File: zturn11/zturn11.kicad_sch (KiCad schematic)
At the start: 138 parts, among them J1 2x18edgecon, J11 Conn_02x40_Odd_Even, J12 Conn_02x40_Odd_Even, J2 2x18edgecon, J3 2x18edgecon, J4 2x18edgecon, J5 Conn_01x16, J7 Conn_01x03, Q1 SSM6N15AFU, Q10 SSM6N15AFU, Q11 SSM6N15AFU, Q12 SSM6N15AFU, Q13 SSM6N15AFU, Q14 SSM6N15AFU, Q15 SSM6N15AFU, Q16 SSM6N15AFU, Q17 SSM6N15AFU, Q18 SSM6N15AFU, Q19 SSM6N15AFU, Q2 SSM6N15AFU, Q20 SSM6N15AFU, Q21 SSM6N15AFU, Q22 SSM6N15AFU, Q23 SSM6N15AFU, Q24 SSM6N15AFU, Q25 SSM6N15AFU, Q26 SSM6N15AFU, Q27 SSM6N15AFU, Q28 SSM6N15AFU, Q29 SSM6N15AFU, Q3 SSM6N15AFU, Q30 SSM6N15AFU, Q31 SSM6N15AFU, Q32 SSM6N15AFU, Q33 SSM6N15AFU, Q34 SSM6N15AFU, Q35 SSM6N15AFU, Q36 SSM6N15AFU, Q37 SSM6N15AFU, Q38 SSM6N15AFU, Q39 SSM6N15AFU, Q4 SSM6N15AFU, Q40 SSM6N15AFU, Q41 SSM6N15AFU, Q42 SSM6N15AFU, Q43 SSM6N15AFU, Q44 SSM6N15AFU, Q5 SSM6N15AFU, Q50 SSM6N15AFU, Q51 SSM6N15AFU, Q52 SSM6N15AFU, Q53 SSM6N15AFU, Q54 SSM6N15AFU, Q55 SSM6N15AFU, Q56 SSM6N15AFU, Q57 SSM6N15AFU, Q58 SSM6N15AFU, Q59 SSM6N15AFU, Q6 SSM6N15AFU, Q60 SSM6N15AFU, Q61 SSM6N15AFU, Q62 SSM6N15AFU, Q63 SSM6N15AFU, Q64 SSM6N15AFU, Q7 SSM6N15AFU, Q8 SSM6N15AFU, Q9 SSM6N15AFU

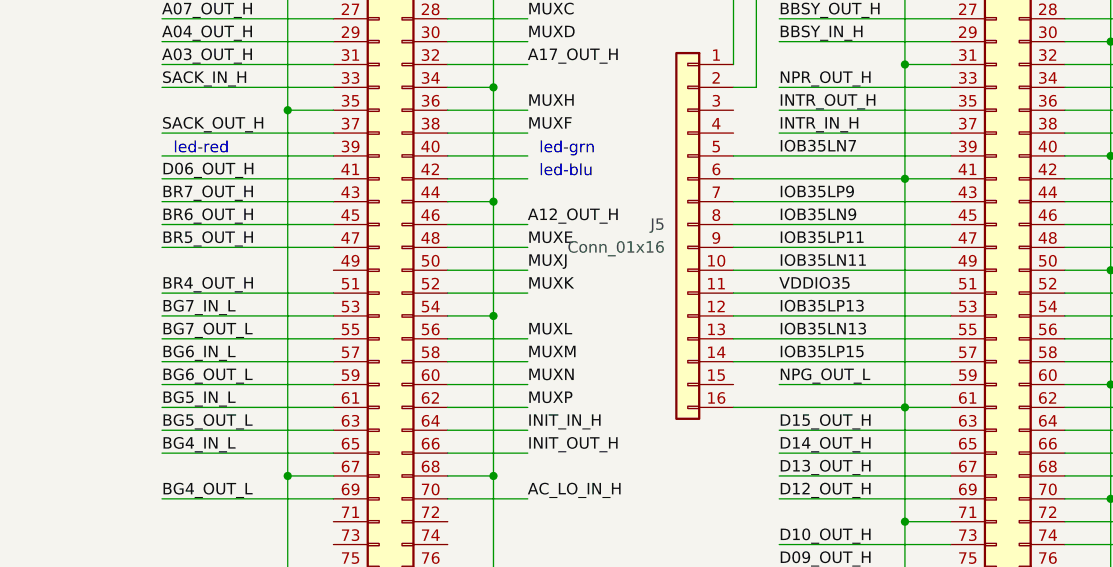
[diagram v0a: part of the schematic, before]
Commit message: update pcb with patch for BG6_OUT_H
also move power connector out from under zturn board
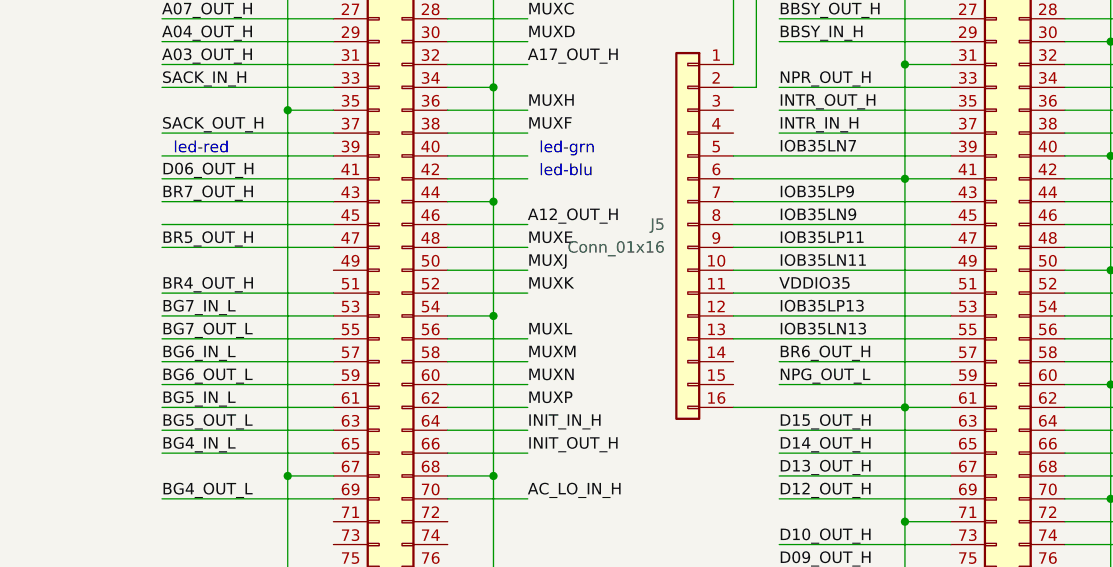
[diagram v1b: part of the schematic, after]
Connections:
- net BR6_OUT_H: now also J12.57 (Pin_57); no longer J11.45 (Pin_45)
- net IOB35LP15: no longer names the net of J5.14 (Pin_14)
- net IOB35LP15: no longer J12.57 (Pin_57)
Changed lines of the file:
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@@
+    (stroke (width 0) (type default))
+  )
+  (wire (pts (xy 334.01 111.76) (xy 353.06 111.76))
     (stroke (width 0) (type default))
   )
@@
     (stroke (width 0) (type default))
   )
-  (wire (pts (xy 328.93 111.76) (xy 353.06 111.76))
-    (stroke (width 0) (type default))
-  )
   (wire (pts (xy 403.86 400.05) (xy 411.48 400.05))
     (stroke (width 0) (type default))
@@
     (effects (font (size 1.27 1.27)) (justify left bottom))
   )
-  (label "IOB35LP15" (at 334.01 111.76 0) (fields_autoplaced)
-    (effects (font (size 1.27 1.27)) (justify left bottom))
-  )
   (label "BUS_A17_L" (at 121.92 27.94 0) (fields_autoplaced)
     (effects (font (size 1.27 1.27)) (justify left bottom))
@@
     (effects (font (size 1.27 1.27)) (justify left bottom))
   )
-  (label "BR6_OUT_H" (at 265.43 96.52 0) (fields_autoplaced)
-    (effects (font (size 1.27 1.27)) (justify left bottom))
-  )
+  (label "BR6_OUT_H" (at 334.01 111.76 0) (fields_autoplaced)
+    (effects (font (size 1.27 1.27)) (justify left bottom))
+  )

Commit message: add diodes to the zturn11 board so the muxes work
also add AC_LO_OUT_H and DC_LO_OUT_H drivers
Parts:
- added C20: 0.1u, Capacitor_SMD:C_0402_1005Metric, symbol Device:C
- added D1, D10, D11, D12, D13, D14, D15, D16, D17, D18, D19, D2, D20, D21, D22, D23, D24, D25, D26, D27, D28, D29, D3, D30, D31, D32, D33, D34, D35, D36, D37, D38, D39, D4, D40, D41, D42, D43, D44, D5, D6, D7, D8, D9: RB521S-30, Diode_SMD:D_SOD-523, symbol Device:D_Schottky_Small
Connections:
- net +3V3: now also J5.4 (Pin_4), C20.1
- net BR6_OUT_H: now also J11.43 (Pin_43); no longer J12.57 (Pin_57)
- net BR7_OUT_H: now also J11.41 (Pin_41); no longer J11.43 (Pin_43)
- net BUS_AC_LO_L: now also Q8.3 (D2)
- net BUS_DC_LO_L: now also Q4.3 (D2)
- net D00_OUT_H: now also J12.58 (Pin_58); no longer J12.56 (Pin_56)
- net D01_OUT_H: now also J12.62 (Pin_62); no longer J12.58 (Pin_58)
- net D02_OUT_H: now also J12.54 (Pin_54); no longer J12.52 (Pin_52)
- net D03_OUT_H: now also J12.56 (Pin_56); no longer J12.54 (Pin_54)
- net D04_OUT_H: now also J12.66 (Pin_66); no longer J12.64 (Pin_64)
- net D05_OUT_H: now also J12.64 (Pin_64); no longer J12.62 (Pin_62)
- net D06_OUT_H: now also J12.52 (Pin_52); no longer J11.41 (Pin_41)
- net D07_OUT_H: now also J12.77 (Pin_77); no longer J12.66 (Pin_66)
- net D08_OUT_H: now also J12.75 (Pin_75); no longer J12.77 (Pin_77)
- net D09_OUT_H: now also J12.73 (Pin_73); no longer J12.75 (Pin_75)
- net D10_OUT_H: now also J12.69 (Pin_69); no longer J12.73 (Pin_73)
- net D11_OUT_H: now also J12.79 (Pin_79); no longer J12.76 (Pin_76)
- net D12_OUT_H: now also J12.67 (Pin_67); no longer J12.69 (Pin_69)
- net D13_OUT_H: now also J12.65 (Pin_65); no longer J12.67 (Pin_67)
- net D14_OUT_H: now also J12.59 (Pin_59); no longer J12.65 (Pin_65)
- net D15_OUT_H: now also J12.55 (Pin_55); no longer J12.63 (Pin_63)
- net DC_LO_IN_H: now also J12.76 (Pin_76); no longer J12.74 (Pin_74)
- net GND: now also C20.2
- net HLTGR_IN_L: now also J12.72 (Pin_72); no longer J12.68 (Pin_68)
- net HLTRQ_OUT_H: now also J12.74 (Pin_74); no longer J12.72 (Pin_72)
- net MUXA: now also D1.2 (A), D5.2 (A), D8.2 (A); no longer Q10.6 (D1), Q14.6 (D1), Q2.6 (D1)
- net MUXB: now also D2.2 (A), D6.2 (A), D9.2 (A); no longer Q11.6 (D1), Q16.6 (D1), Q3.6 (D1)
- net MUXC: now also D10.2 (A), D3.2 (A), D7.2 (A); no longer Q13.6 (D1), Q17.6 (D1), Q5.6 (D1)
- net MUXD: now also D11.2 (A), D27.2 (A), D4.2 (A); no longer Q18.6 (D1), Q36.6 (D1), Q7.6 (D1)
- net MUXE: now also D12.2 (A), D23.2 (A), D28.2 (A); no longer Q19.6 (D1), Q25.6 (D1), Q37.6 (D1)
- net MUXF: now also D13.2 (A), D22.2 (A), D29.2 (A); no longer Q20.6 (D1), Q26.6 (D1), Q38.6 (D1)
- net MUXH: now also D14.2 (A), D21.2 (A), D30.2 (A); no longer Q21.6 (D1), Q27.6 (D1), Q39.6 (D1)
- net MUXJ: now also D15.2 (A), D20.2 (A), D31.2 (A); no longer Q23.6 (D1), Q28.6 (D1), Q40.6 (D1)
- net MUXK: now also D19.2 (A), D35.2 (A), D42.2 (A); no longer Q29.6 (D1), Q41.6 (D1), Q57.6 (D1)
- net MUXL: now also D18.2 (A), D36.2 (A), D43.2 (A); no longer Q30.6 (D1), Q42.6 (D1), Q58.6 (D1)
- net MUXM: now also D17.2 (A), D37.2 (A), D44.2 (A); no longer Q31.6 (D1), Q43.6 (D1), Q59.6 (D1)
- net MUXN: now also D16.2 (A), D34.2 (A), D38.2 (A); no longer Q32.6 (D1), Q54.6 (D1), Q60.6 (D1)
- net MUXP: now also D24.2 (A), D33.2 (A), D39.2 (A); no longer Q33.6 (D1), Q55.6 (D1), Q61.6 (D1)
- net MUXR: now also D25.2 (A), D32.2 (A), D40.2 (A); no longer Q34.6 (D1), Q56.6 (D1), Q62.6 (D1)
- net MUXS: now also D26.2 (A), D41.2 (A); no longer Q35.6 (D1), Q63.6 (D1)
- net NPG_IN_L: now also J12.57 (Pin_57); no longer J12.79 (Pin_79)
- net NPG_OUT_L: now also J12.53 (Pin_53); no longer J12.59 (Pin_59)
- net PA_OUT_H: now also J12.63 (Pin_63); no longer J12.78 (Pin_78)
- net PB_OUT_H: now also J12.48 (Pin_48); no longer J12.46 (Pin_46)
- net RSEL1_H: now also J12.68 (Pin_68); no longer J12.48 (Pin_48)
- net DC_LO_OUT_H: now reaches Q4.5 (G2)
- net DC_LO_OUT_H: now also J12.78 (Pin_78)
- net AC_LO_OUT_H: now reaches Q8.5 (G2)
- net AC_LO_OUT_H: now also J12.46 (Pin_46)
- net IOB35LN13: no longer names the net of J5.13 (Pin_13)
- net IOB35LN13: no longer J12.55 (Pin_55)
- net IOB35LP13: no longer names the net of J5.12 (Pin_12)
- net IOB35LP13: no longer J12.53 (Pin_53)
- new net: D38.1 (K), Q60.6 (D1)
- new net: D4.1 (K), Q7.6 (D1)
- new net: D41.1 (K), Q63.6 (D1)
- new net: D29.1 (K), Q38.6 (D1)
- new net: D31.1 (K), Q40.6 (D1)
- new net: D14.1 (K), Q21.6 (D1)
- new net: D24.1 (K), Q33.6 (D1)
- new net: D27.1 (K), Q36.6 (D1)
- new net: D6.1 (K), Q11.6 (D1)
- new net: D3.1 (K), Q5.6 (D1)
- new net: D28.1 (K), Q37.6 (D1)
- new net: D16.1 (K), Q32.6 (D1)
- new net: D39.1 (K), Q61.6 (D1)
- new net: D17.1 (K), Q31.6 (D1)
- new net: D10.1 (K), Q17.6 (D1)
- new net: D8.1 (K), Q14.6 (D1)
- new net: D11.1 (K), Q18.6 (D1)
- new net: D15.1 (K), Q23.6 (D1)
- new net: D20.1 (K), Q28.6 (D1)
- new net: D26.1 (K), Q35.6 (D1)
- new net: D40.1 (K), Q62.6 (D1)
- new net: D13.1 (K), Q20.6 (D1)
- new net: D1.1 (K), Q2.6 (D1)
- new net: D30.1 (K), Q39.6 (D1)
- new net: D21.1 (K), Q27.6 (D1)
- new net: D23.1 (K), Q25.6 (D1)
- new net: D32.1 (K), Q56.6 (D1)
- new net: D5.1 (K), Q10.6 (D1)
- new net: D2.1 (K), Q3.6 (D1)
- new net: D44.1 (K), Q43.6 (D1)
- new net: D19.1 (K), Q29.6 (D1)
- new net: D22.1 (K), Q26.6 (D1)
- new net: D18.1 (K), Q30.6 (D1)
- new net: D42.1 (K), Q41.6 (D1)
- new net: D25.1 (K), Q34.6 (D1)
- new net: D35.1 (K), Q57.6 (D1)
- new net: D9.1 (K), Q16.6 (D1)
- new net: D12.1 (K), Q19.6 (D1)
- new net: D37.1 (K), Q59.6 (D1)
- new net: D33.1 (K), Q55.6 (D1)
- new net: D7.1 (K), Q13.6 (D1)
- new net: D43.1 (K), Q42.6 (D1)
- new net: D36.1 (K), Q58.6 (D1)
- new net: D34.1 (K), Q54.6 (D1)
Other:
- moved on the sheet: C13, C14, C15, C16, C17, C18, C19
